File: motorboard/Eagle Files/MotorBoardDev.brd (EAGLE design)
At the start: 86 x 80.5 mm, 77 parts, among them J1 Under Glow, J2 B2PS-VH(LF)(SN), J3 B2PS-VH(LF)(SN), J4 B2PS-VH(LF)(SN), J5 B2PS-VH(LF)(SN), Q4 STT4P3LLH6, Q5 RRH100P03GZETB, T1 R-78E5.0-1.0, U1 9DoF IMU, U2 TXB0104DR, U4 TLV70233DBVR, U5 TC4427ACOA713, U6 TC4427ACOA713, U7 TC4427ACOA713, X1 MINI-USB_SHIELD5P4-32005-400, X2 C-GRID-05-15-91, X3 2510-, X4 2510-, X5 C-GRID-05-15-91, X6 C-GRID-02-70553, X7 SI-50170

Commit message: Finalized and should be ready to order
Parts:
- added J6: B2PS-VH(LF)(SN), RoboJackets-Connectors:B2PS-CENTERED
- U2: value TXB0104DR -> TXB0106PWR; device MotorBoardDev:D14 -> MotorBoardDev:PW16
- moved U2 21.5 mm to (45.0, 26.4)
- moved U1 12.3 mm to (22.2, 64.6)
- moved C2 12.2 mm to (25.7, 64.5)
- moved R11 12.2 mm to (18.6, 64.5)
- moved R8 12.1 mm to (28.1, 64.5)
- moved C3 11.3 mm to (21.1, 61.2)
- moved R1 7.53 mm to (21.2, 58.1), turned to 0 degrees
- moved D1 3.40 mm to (24.6, 58.1)
- moved R18 1.74 mm to (14.2, 57.1), turned to 270 degrees
- moved D3 1.42 mm to (14.2, 61.3), turned to 90 degrees
- moved U$14 0.94 mm to (68.3, 33.0)
- moved C8 0.71 mm to (48.6, 69.9), flipped to the top
- moved X5 0.45 mm to (83.0, 21.0)
- moved U$7 0.35 mm to (54.7, 10.2)
- moved U$8 0.35 mm to (32.5, 10.2)
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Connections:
- new net MOTOR_CTRL: J6.2, U2.16
- new net MOTOR_CTRL_3V3: A1.13, U2.1
- net +3V3: now also U2.2; no longer U2.1
- net +5V: now also U2.15; no longer U2.14
- net BLUE_3V3: now also A1.16; no longer A1.15
- net FRONT_LIGHT_3V3: now also A1.17; no longer A1.16
- net GND: now also J6.1, U2.9; no longer U2.7
- net GREEN_3V3: now also A1.15; no longer A1.14
- net LEA: now also U2.12; no longer U2.11
- net LEA3: now also U2.5; no longer U2.4
- net LEB: now also U2.11; no longer U2.10
- net LEB3: now also U2.6; no longer U2.5
- net REA: now also U2.14; no longer U2.13
- net REA3: now also U2.3; no longer U2.2
- net REB: now also U2.13; no longer U2.12
- net REB3: now also U2.4; no longer U2.3
- net RED_3V3: now also A1.14; no longer A1.13
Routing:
- net MOTOR_CTRL: track 0.00 -> 72.3 mm, vias 0 -> 3
- net MOTOR_CTRL_3V3: track 0.00 -> 27.8 mm, vias 0 -> 1
- net REA: track 8.97 -> 33.0 mm, vias 0 -> 2
- net REB3: track 7.73 -> 28.6 mm
- net REA3: track 9.97 -> 30.2 mm
- net LEA3: track 6.80 -> 26.7 mm
- net LEB3: track 5.43 -> 24.8 mm
- net +3V3: track 38.3 -> 56.3 mm, vias 3 -> 1
- net GYRO_INT: track 33.7 -> 18.3 mm
- net SCL: track 38.8 -> 24.4 mm
- net REB: track 13.2 -> 27.3 mm, vias 0 -> 2
- net SDA: track 39.5 -> 26.6 mm
- net LEA: track 24.1 -> 33.1 mm
- net FRONT_LIGHT_3V3: track 25.3 -> 28.9 mm
- net INDICATOR_LED: track 5.73 -> 8.83 mm
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
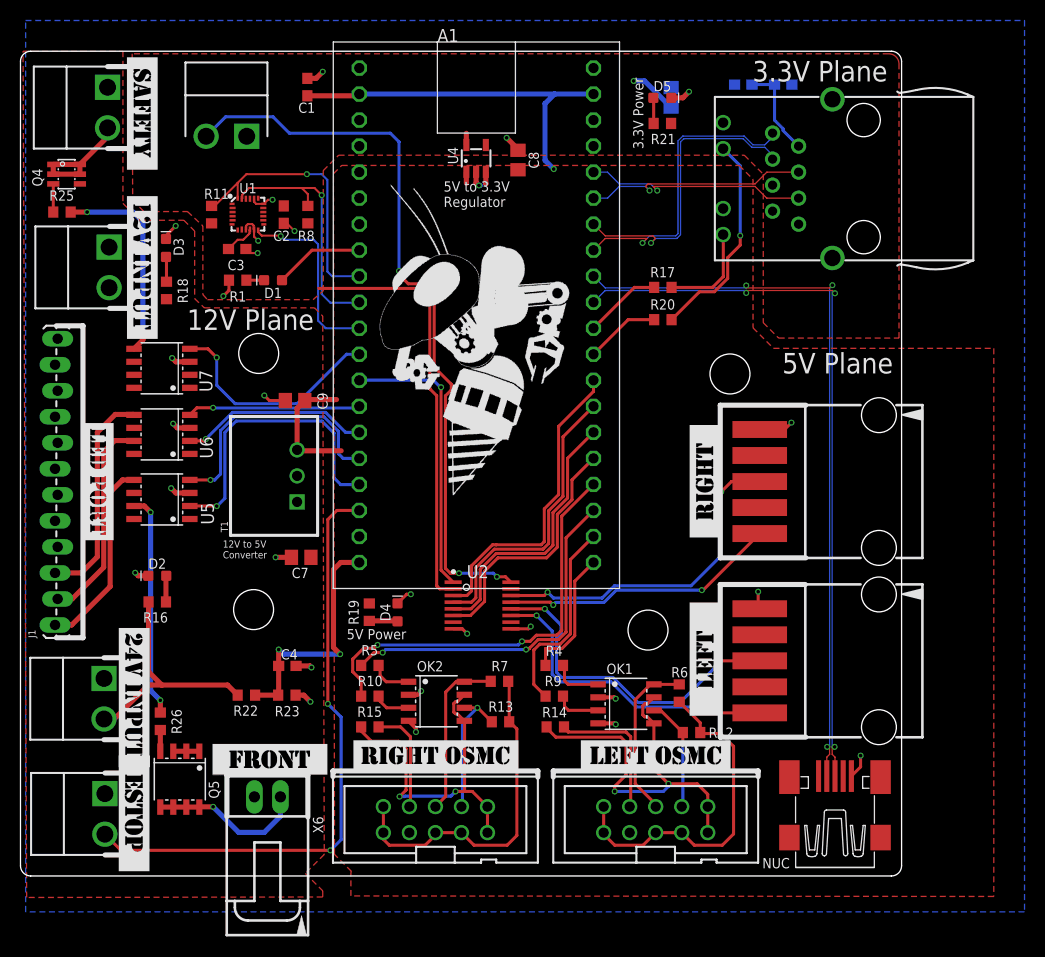
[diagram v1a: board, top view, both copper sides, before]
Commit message: Silk Screen fixed
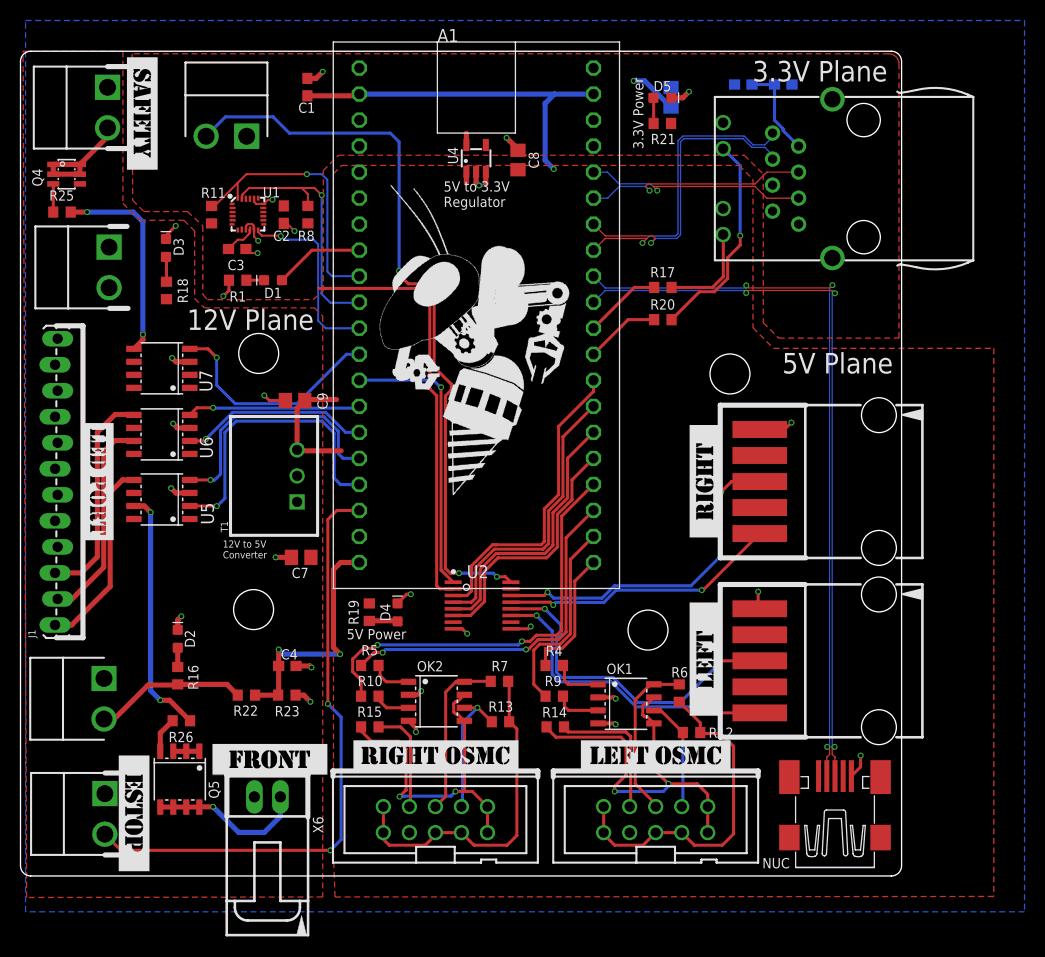
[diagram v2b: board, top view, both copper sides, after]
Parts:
- added U$16: (no value), MotorBoardDev:STMC
- U$5: device MotorBoardDev:12VINPUT -> MotorBoardDev:12V
- U$6: device MotorBoardDev:24VINPUT -> MotorBoardDev:24V
- moved R16 7.47 mm to (15.3, 19.6), turned to 270 degrees
- moved D2 6.47 mm to (15.3, 23.1), turned to 90 degrees
- moved U$6 4.00 mm to (9.80, 20.2)
- moved U$5 3.85 mm to (10.5, 62.5)
- moved R26 2.05 mm to (15.7, 15.2), turned to 180 degrees
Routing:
- net +24V: track 23.5 -> 14.9 mm
- net FRONT_LIGHT: track 21.8 -> 24.4 mm
- net FRONT_R: track 2.08 -> 3.48 mm
- net 24V_LED_R: track 2.56 -> 1.95 mm

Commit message: mbed test code and eagle side-notes
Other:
- outline, holes or cut-outs redrawn
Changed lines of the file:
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@@
 <?xml version="1.0" encoding="utf-8"?>
 <!DOCTYPE eagle SYSTEM "eagle.dtd">
-<eagle version="8.4.2">
+<eagle version="8.5.2">
 <drawing>
 <settings>
@@
 <board>
 <plain>
-<wire x1="0" y1="79.5" x2="0" y2="1" width="0" layer="20"/>
-<wire x1="0" y1="1" x2="1" y2="0" width="0" layer="20" curve="90"/>
-<wire x1="1" y1="0" x2="85" y2="0" width="0" layer="20"/>
-<wire x1="85" y1="0" x2="86" y2="1" width="0" layer="20" curve="90"/>
-<wire x1="86" y1="1" x2="86" y2="79.5" width="0" layer="20"/>
-<wire x1="86" y1="79.5" x2="85" y2="80.5" width="0" layer="20" curve="90"/>
-<wire x1="85" y1="80.5" x2="1" y2="80.5" width="0" layer="20"/>
-<wire x1="1" y1="80.5" x2="0" y2="79.5" width="0" layer="20" curve="90"/>
+<wire x1="83" y1="80.5" x2="3" y2="80.5" width="0" layer="20"/>
+<wire x1="3" y1="80.5" x2="0" y2="77.5" width="0" layer="20" curve="90"/>
+<wire x1="0" y1="77.5" x2="0" y2="3" width="0" layer="20"/>
+<wire x1="0" y1="3" x2="3" y2="0" width="0" layer="20" curve="90"/>
+<wire x1="3" y1="0" x2="83" y2="0" width="0" layer="20"/>
+<wire x1="83" y1="0" x2="86" y2="3" width="0" layer="20" curve="90"/>
+<wire x1="86" y1="3" x2="86" y2="77.5" width="0" layer="20"/>
+<wire x1="86" y1="77.5" x2="83" y2="80.5" width="0" layer="20" curve="90"/>
 <text x="71.45" y="77.55" size="2" layer="21">3.3V Plane</text>
 <text x="74.35" y="49.05" size="2" layer="21">5V Plane</text>
@@
 <param name="checkRestrict" value="1"/>
 <param name="checkStop" value="0"/>
+<param name="checkValues" value="0"/>
 <param name="useDiameter" value="13"/>
 <param name="maxErrors" value="50"/>
@@
 <vertex x="74" y="52.5"/>
 <vertex x="85.75" y="52.5"/>
-<vertex x="85.75" y="79.25" curve="90"/>
-<vertex x="84.75" y="80.25"/>
+<vertex x="85.75" y="77.25" curve="90"/>
+<vertex x="82.75" y="80.25"/>
 <vertex x="10.9" y="80.25"/>
 <vertex x="10.95" y="65.95"/>

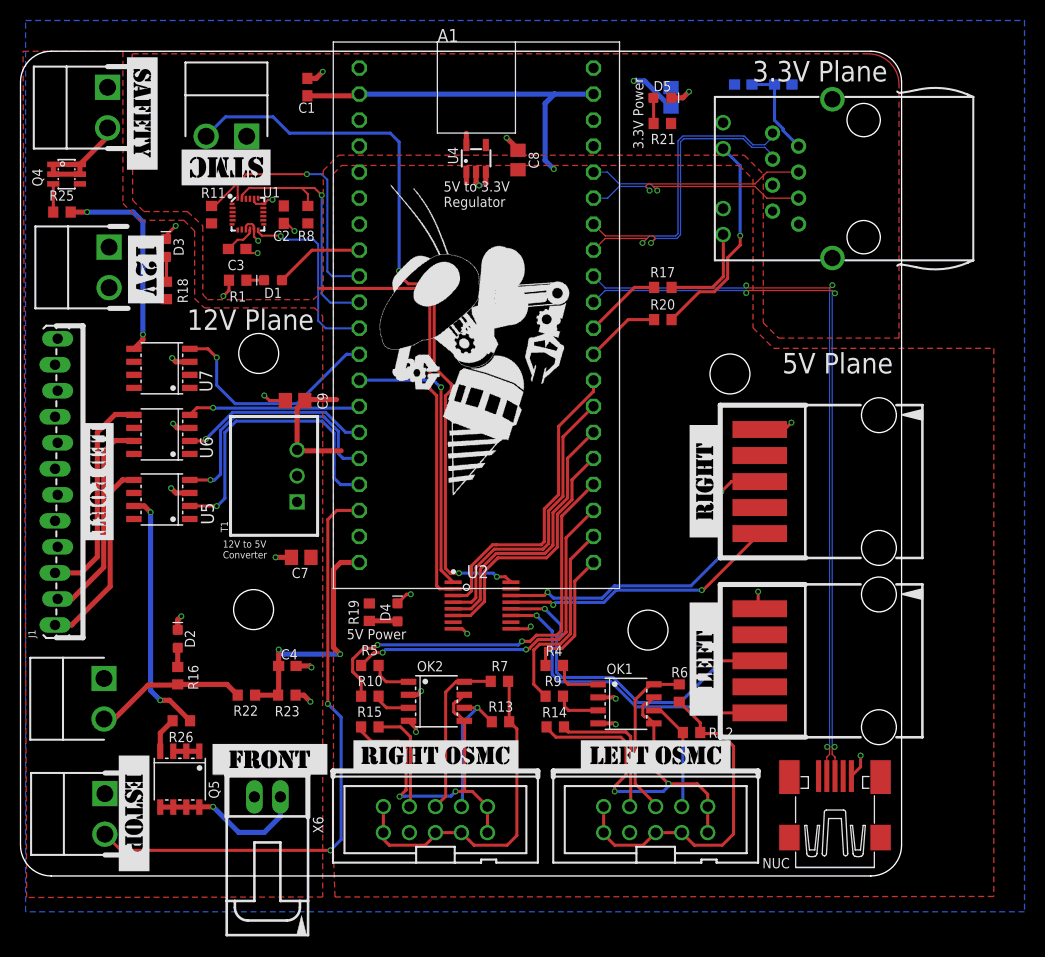
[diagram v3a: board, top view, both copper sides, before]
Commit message: Schematics update and Control code initial commit
Updated Motor board schematics with regard to the level shifter OE pin;
Initial commit to the migration of arduino code for motor shield to motor board.
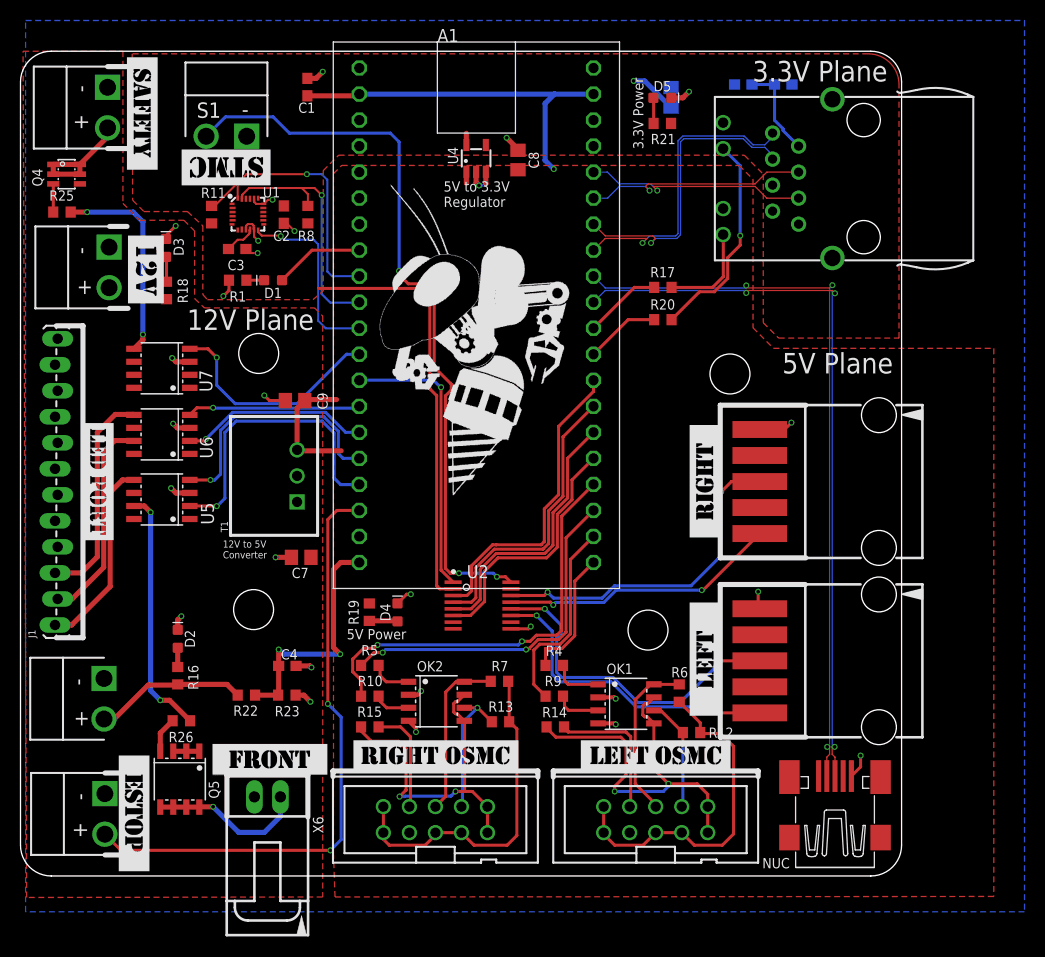
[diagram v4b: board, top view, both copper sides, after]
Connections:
- net GND: no longer U2.8
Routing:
- net GND: track 51.7 -> 50.1 mm, vias 28 -> 27
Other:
- board text added: "+"
- board text added: "-"
- board text added: "S1"
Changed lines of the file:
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@@
 <?xml version="1.0" encoding="utf-8"?>
 <!DOCTYPE eagle SYSTEM "eagle.dtd">
-<eagle version="8.5.2">
+<eagle version="8.6.0">
 <drawing>
 <settings>
@@
 <wire x1="9.8" y1="13.3" x2="9.8" y2="21.3" width="0.5" layer="103"/>
 <wire x1="9.8" y1="21.3" x2="8.1" y2="21.3" width="0.5" layer="103"/>
+<text x="5.5" y="56.8" size="1.5" layer="25" font="vector" ratio="10">+</text>
+<text x="6.6" y="60.7" size="1.5" layer="25" font="vector" ratio="10" rot="R90">-</text>
+<text x="6.3" y="18.6" size="1.5" layer="25" font="vector" ratio="10" rot="R90">-</text>
+<text x="5.2" y="14.7" size="1.5" layer="25" font="vector" ratio="10">+</text>
+<text x="6.5" y="7.4" size="1.5" layer="25" font="vector" ratio="10" rot="R90">-</text>
+<text x="21.6" y="74.1" size="1.5" layer="25" font="vector" ratio="10">-</text>
+<text x="17.2" y="74" size="1.5" layer="25" font="vector" ratio="10">S1</text>
+<text x="6.6" y="76.5" size="1.5" layer="25" font="vector" ratio="10" rot="R90">-</text>
+<text x="6.6" y="72.8" size="1.5" layer="25" font="vector" ratio="10" rot="R90">+</text>
+<text x="6.5" y="3.7" size="1.5" layer="25" font="vector" ratio="10" rot="R90">+</text>
 </plain>
 <attributes>
@@
 <via x="23.2" y="62" extent="1-16" drill="0.35"/>
 <contactref element="U2" pad="9"/>
-<contactref element="U2" pad="8"/>
 <wire x1="47.8694" y1="24.125" x2="49.575" y2="24.125" width="0.3" layer="1"/>
 <wire x1="49.575" y1="24.125" x2="49.8" y2="24.35" width="0.3" layer="1"/>
 <via x="49.8" y="24.35" extent="1-16" drill="0.35"/>
-<wire x1="42.2306" y1="24.125" x2="43.125" y2="24.125" width="0.3" layer="1"/>
-<wire x1="43.125" y1="24.125" x2="43.6" y2="23.65" width="0.3" layer="1"/>
-<via x="43.6" y="23.65" extent="1-16" drill="0.35"/>
 <wire x1="72.155" y1="43.58" x2="74.58" y2="43.58" width="0.3" layer="1"/>
 <wire x1="48.56" y1="70.83" x2="48.56" y2="70.94" width="0.5" layer="1"/>
